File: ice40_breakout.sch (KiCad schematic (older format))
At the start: 0 parts

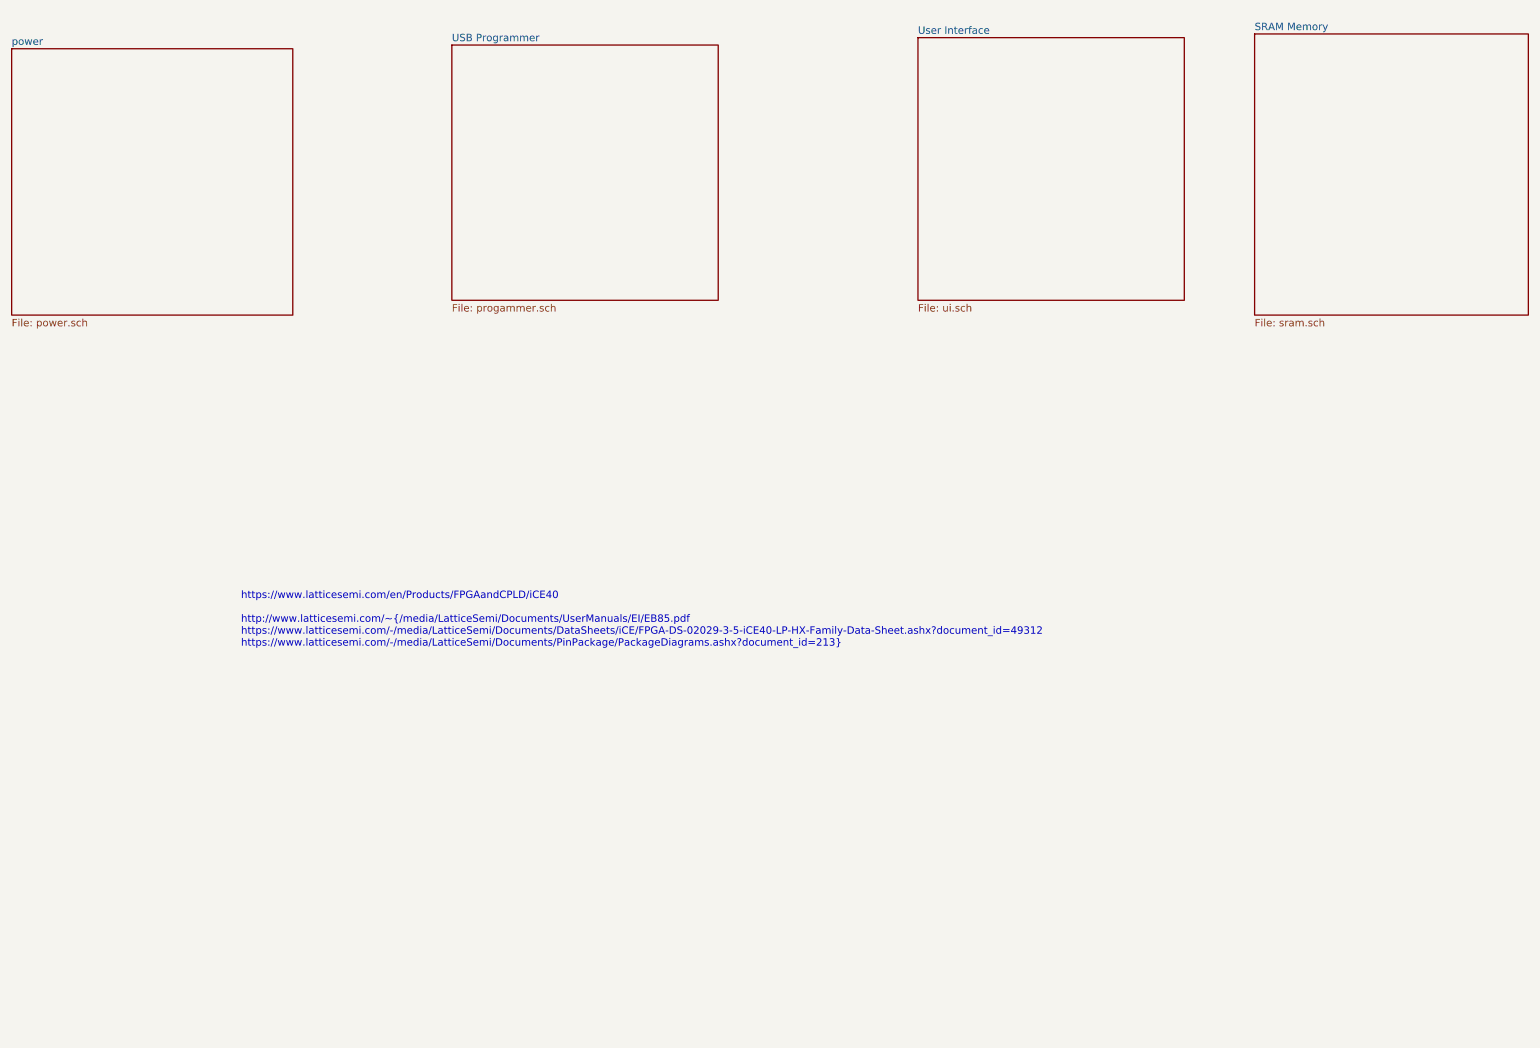
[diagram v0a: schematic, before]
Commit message: Made a overview on the toplevel schematic and added the SRAM subschematic.
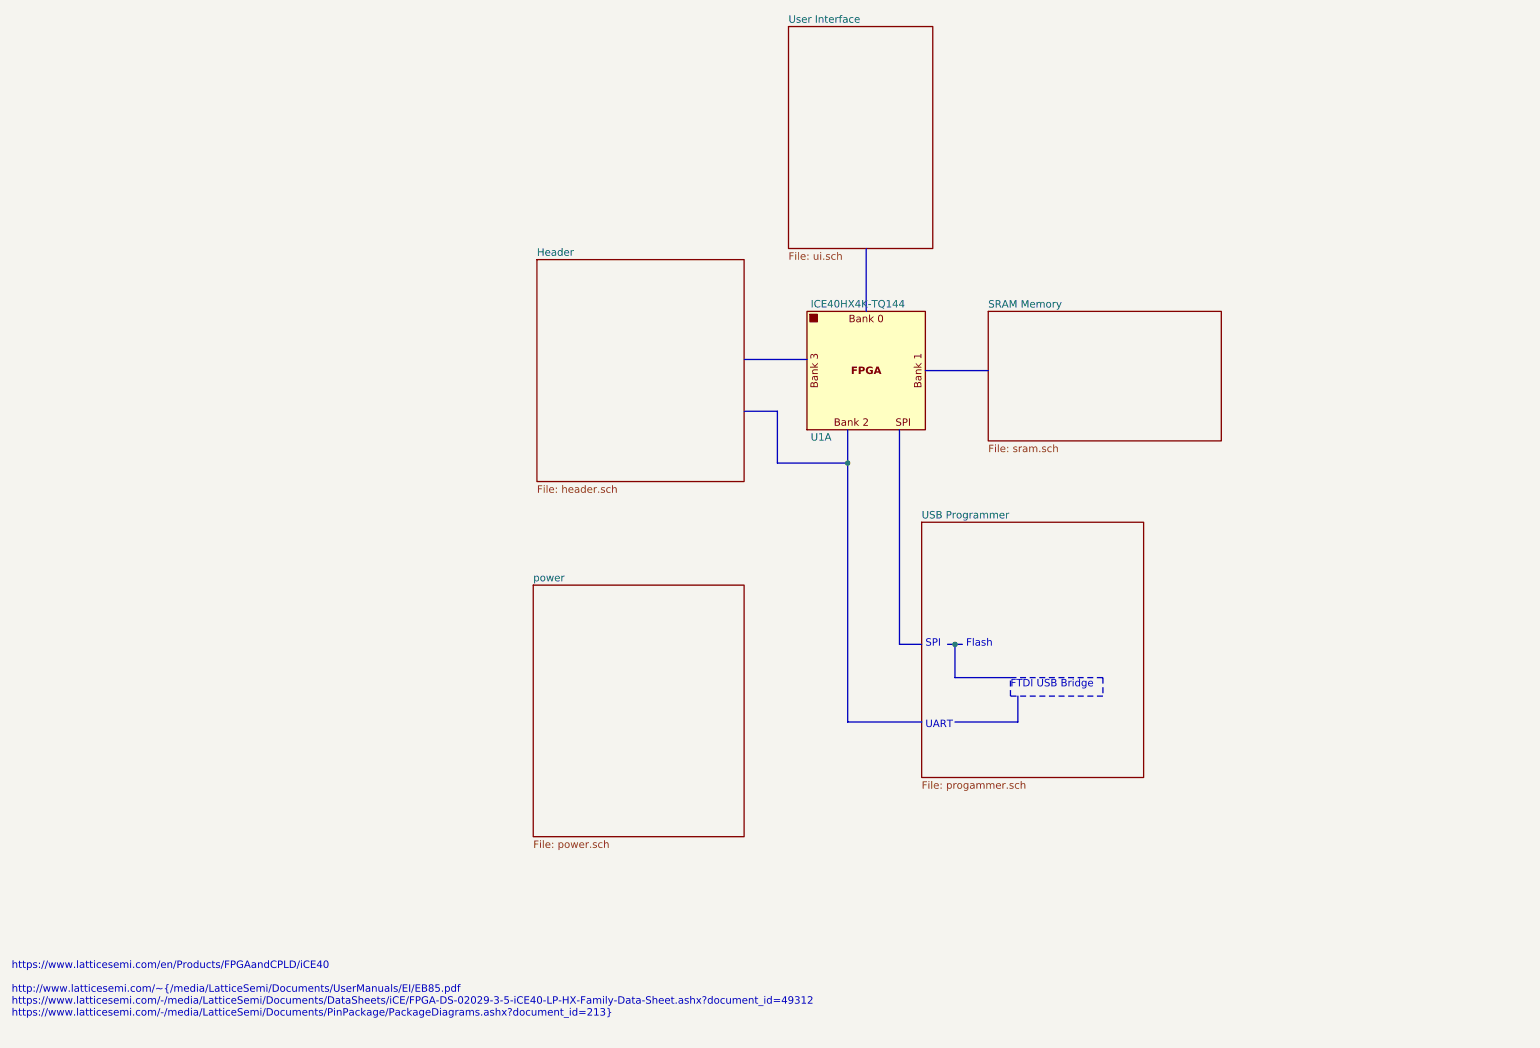
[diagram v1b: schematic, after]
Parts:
- added U1: ICE40HX4K-TQ144, Package_QFP:TQFP-144_20x20mm_P0.5mm, symbol ice40hx4k:ICE40HX4K-TQ144
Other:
- note added: "FTDI USB Bridge"
- note added: "Flash"
- note added: "SPI"
- note added: "UART"
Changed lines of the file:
@@
 EESchema Schematic File Version 4
+LIBS:ice40_breakout-cache
 EELAYER 29 0
 EELAYER END
 $Descr A4 11693 8268
 encoding utf-8
-Sheet 1 5
+Sheet 1 6
 Title ""
 Date ""
@@
 $EndDescr
 $Sheet
-S 550  925  1900 1800
+S 4075 4550 1425 1700
 U 5CA8FBC7
 F0 "power" 50
@@
 $EndSheet
 $Sheet
-S 6675 850  1800 1775
+S 5800 775  975  1500
 U 5CAB7CD4
 F0 "User Interface" 50
 F1 "ui.sch" 50
 $EndSheet
-Text Notes 2100 4975 0    50   ~ 0
+Text Notes 550  7475 0    50   ~ 0
 https://www.latticesemi.com/en/Products/FPGAandCPLD/iCE40\n\nhttp://www.latticesemi.com/~/media/LatticeSemi/Documents/UserManuals/EI/EB85.pdf\nhttps://www.latticesemi.com/-/media/LatticeSemi/Documents/DataSheets/iCE/FPGA-DS-02029-3-5-iCE40-LP-HX-Family-Data-Sheet.ashx?document_id=49312\nhttps://www.latticesemi.com/-/media/LatticeSemi/Documents/PinPackage/PackageDiagrams.ashx?document_id=213
 $Sheet
-S 3525 900  1800 1725
+S 7150 2700 1575 875
+U 5CADFC7F
+F0 "SRAM Memory" 50
+F1 "sram.sch" 50
+$EndSheet
+$Comp
+L ice40hx4k:ICE40HX4K-TQ144 U1
+U 1 1 5CB278E5
+P 6325 3100
+F 0 "U1" H 5950 2650 50  0000 L CNN
+F 1 "ICE40HX4K-TQ144" H 5950 3550 50  0000 L CNN
+F 2 "Package_QFP:TQFP-144_20x20mm_P0.5mm" H 6325 3100 50  0001 C CNN
+F 3 "" H 6325 3100 50  0001 C CNN
+	1    6325 3100
+	1    0    0    -1
+$EndComp
+Wire Bus Line
+	6550 3500 6550 4950
+Wire Bus Line
+	6550 4950 6700 4950
+Wire Bus Line
+	6725 3100 7150 3100
+Wire Bus Line
+	6325 2700 6325 2275
+Text Notes 6725 4975 0    50   ~ 0
+SPI
+Text Notes 7000 4975 0    50   ~ 0
+Flash
+Text Notes 6725 5525 0    50   ~ 0
+UART
+Wire Bus Line
+	6700 5475 6200 5475
+Wire Bus Line
+	6200 5475 6200 3725
+Wire Bus Line
+	6875 4950 6925 4950
+Text Notes 7300 5250 0    50   ~ 0
+FTDI USB Bridge
+Wire Bus Line
+	6925 4950 6925 5175
+Wire Bus Line
+	6925 5175 7300 5175
+Connection ~ 6925 4950
+Wire Bus Line
+	6925 4950 6975 4950
+Wire Bus Line
+	6925 5475 7350 5475
+Wire Bus Line
+	7350 5475 7350 5300
+Wire Notes Line
+	7300 5175 7925 5175
+Wire Notes Line
+	7925 5175 7925 5300
+Wire Notes Line
+	7925 5300 7300 5300
+Wire Notes Line
+	7300 5300 7300 5175
+$Sheet
+S 6700 4125 1500 1725
 U 5CAB8B22
 F0 "USB Programmer" 50
@@
 $EndSheet
 $Sheet
-S 8950 825  1850 1900
-U 5CADFC7F
-F0 "SRAM Memory" 50
-F1 "sram.sch" 50
+S 4100 2350 1400 1500
+U 5CB5889B
+F0 "Header" 50
+F1 "header.sch" 50
 $EndSheet
+Wire Bus Line
+	5925 3025 5500 3025
+Wire Bus Line
+	6200 3725 5725 3725
+Wire Bus Line
+	5725 3725 5725 3375
+Wire Bus Line
+	5725 3375 5500 3375
+Connection ~ 6200 3725
+Wire Bus Line
+	6200 3725 6200 3500
 $EndSCHEMATC

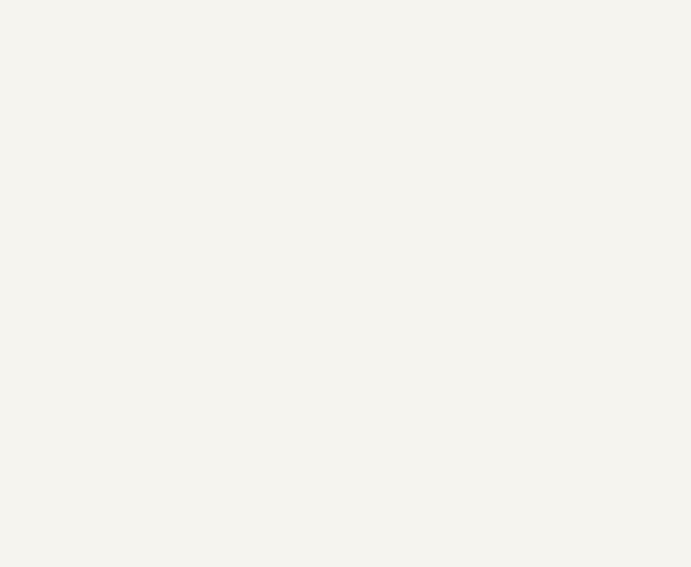
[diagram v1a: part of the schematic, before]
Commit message: sram, ui, power, flash and header
SRAM: mostly done. Changed the choosen IC to a faster one in a differenc housing.

POWER: added some step down converter for 3.3 V and 1.2 V. The 1.2 V is oversized and could be changed to a smaller one

Programmer: added flash.

HEADER: Added Arduino Uno like headers with 5 V signal level. Analog is not connected now, will get an I2C ADC in future. Also added 3 digilent pmod styled connector with 3.3 V signal level.

UI: added 5 buttons and 8 LEDs. There is some space left over, maybe double the LED count in future.
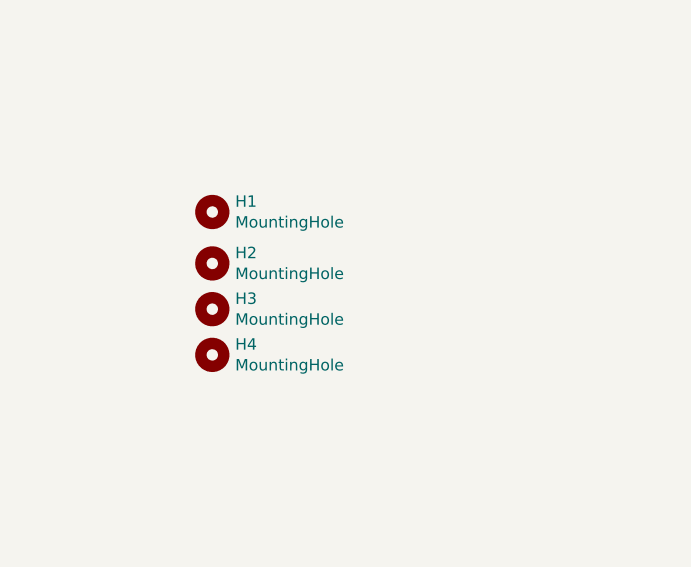
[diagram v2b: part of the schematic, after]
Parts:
- added H1, H2, H3, H4: MountingHole, MountingHole:MountingHole_3mm, symbol Mechanical:MountingHole
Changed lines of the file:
@@
 Wire Bus Line
 	6200 3725 6200 3500
+$Comp
+L Mechanical:MountingHole H1
+U 1 1 5CBF1383
+P 1400 1750
+F 0 "H1" H 1500 1796 50  0000 L CNN
+F 1 "MountingHole" H 1500 1705 50  0000 L CNN
+F 2 "MountingHole:MountingHole_3mm" H 1400 1750 50  0001 C CNN
+F 3 "~" H 1400 1750 50  0001 C CNN
+	1    1400 1750
+	1    0    0    -1
+$EndComp
+$Comp
+L Mechanical:MountingHole H2
+U 1 1 5CBF174A
+P 1400 1975
+F 0 "H2" H 1500 2021 50  0000 L CNN
+F 1 "MountingHole" H 1500 1930 50  0000 L CNN
+F 2 "MountingHole:MountingHole_3mm" H 1400 1975 50  0001 C CNN
+F 3 "~" H 1400 1975 50  0001 C CNN
+	1    1400 1975
+	1    0    0    -1
+$EndComp
+$Comp
+L Mechanical:MountingHole H3
+U 1 1 5CBF1927
+P 1400 2175
+F 0 "H3" H 1500 2221 50  0000 L CNN
+F 1 "MountingHole" H 1500 2130 50  0000 L CNN
+F 2 "MountingHole:MountingHole_3mm" H 1400 2175 50  0001 C CNN
+F 3 "~" H 1400 2175 50  0001 C CNN
+	1    1400 2175
+	1    0    0    -1
+$EndComp
+$Comp
+L Mechanical:MountingHole H4
+U 1 1 5CBF1CC2
+P 1400 2375
+F 0 "H4" H 1500 2421 50  0000 L CNN
+F 1 "MountingHole" H 1500 2330 50  0000 L CNN
+F 2 "MountingHole:MountingHole_3mm" H 1400 2375 50  0001 C CNN
+F 3 "~" H 1400 2375 50  0001 C CNN
+	1    1400 2375
+	1    0    0    -1
+$EndComp
 $EndSCHEMATC

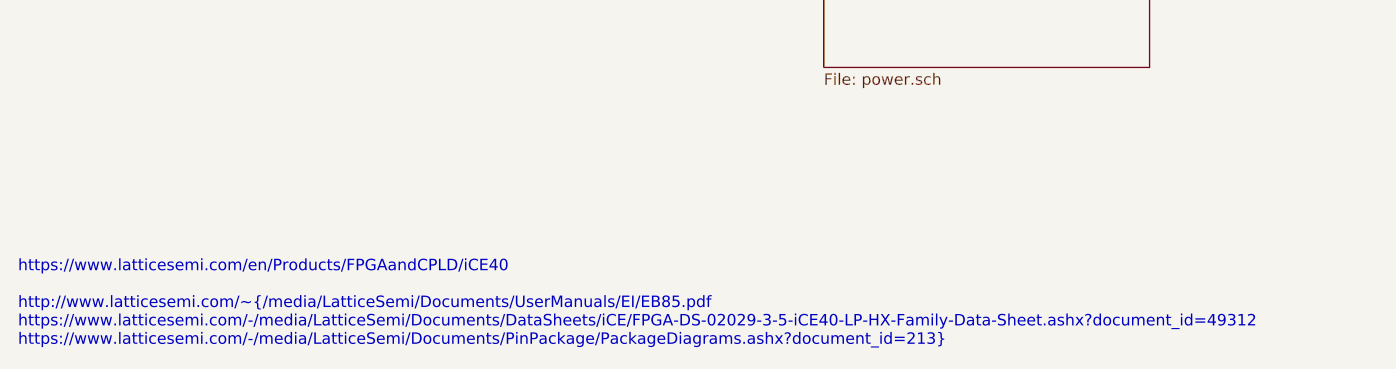
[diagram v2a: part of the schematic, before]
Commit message: Progress on FTDI - added Oscillator and 1.8 V supply
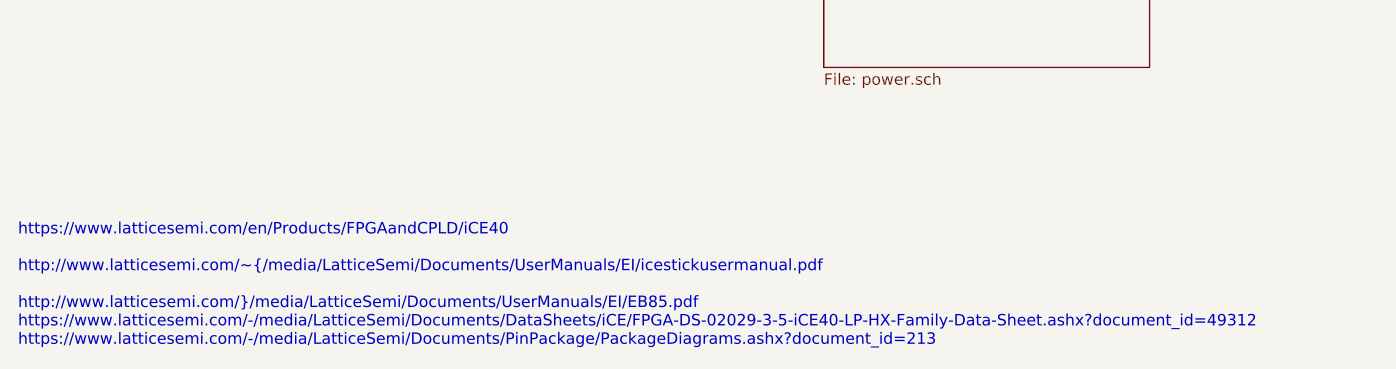
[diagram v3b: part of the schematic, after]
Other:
- note added: "https://www.latticesemi.com/en/Products/FPGAandCPLD/iCE40\n\nhttp://www.latticesemi.com/~/media/LatticeSemi/Documents/UserManuals/EI/icestickusermanual.pdf\n\nhttp://www.latticesemi.com/~/media/LatticeSemi/Documents/UserManuals/EI/EB85.pdf\nhttps://www.latticesemi.com/-/media/LatticeSemi/Documents/DataSheets/iCE/FPGA-DS-02029-3-5-iCE40-LP-HX-Family-Data-Sheet.ashx?document_id=49312\nhttps://www.l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"
- note removed: "https://www.latticesemi.com/en/Products/FPGAandCPLD/iCE40\n\nhttp://www.latticesemi.com/~/media/LatticeSemi/Documents/UserManuals/EI/EB85.pdf\nhttps://www.latticesemi.com/-/media/LatticeSemi/Documents/DataSheets/iCE/FPGA-DS-02029-3-5-iCE40-LP-HX-Family-Data-Sheet.ashx?document_id=49312\nhttps://www.latticesemi.com/-/media/LatticeSemi/Documents/PinPackage/PackageDiagrams.ashx?document_id=213"
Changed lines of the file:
@@
 $EndSheet
 Text Notes 550  7475 0    50   ~ 0
-https://www.latticesemi.com/en/Products/FPGAandCPLD/iCE40\n\nhttp://www.latticesemi.com/~/media/LatticeSemi/Documents/UserManuals/EI/EB85.pdf\nhttps://www.latticesemi.com/-/media/LatticeSemi/Documents/DataSheets/iCE/FPGA-DS-02029-3-5-iCE40-LP-HX-Family-Data-Sheet.ashx?document_id=49312\nhttps://www.latticesemi.com/-/media/LatticeSemi/Documents/PinPackage/PackageDiagrams.ashx?document_id=213
+https://www.latticesemi.com/en/Products/FPGAandCPLD/iCE40\n\nhttp://www.latticesemi.com/~/media/LatticeSemi/Documents/UserManuals/EI/icestickusermanual.pdf\n\nhttp://www.latticesemi.com/~/media/LatticeSemi/Documents/UserManuals/EI/EB85.pdf\nhttps://www.latticesemi.com/-/media/LatticeSemi/Documents/DataSheets/iCE/FPGA-DS-02029-3-5-iCE40-LP-HX-Family-Data-Sheet.ashx?document_id=49312\nhttps://www.latticesemi.com/-/media/LatticeSemi/Documents/PinPackage/PackageDiagrams.ashx?document_id=213
 $Sheet
 S 7150 2700 1575 875
